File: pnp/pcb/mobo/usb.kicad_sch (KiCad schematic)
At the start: 5 parts, among them J9 USB_B, U8 SRV05-4

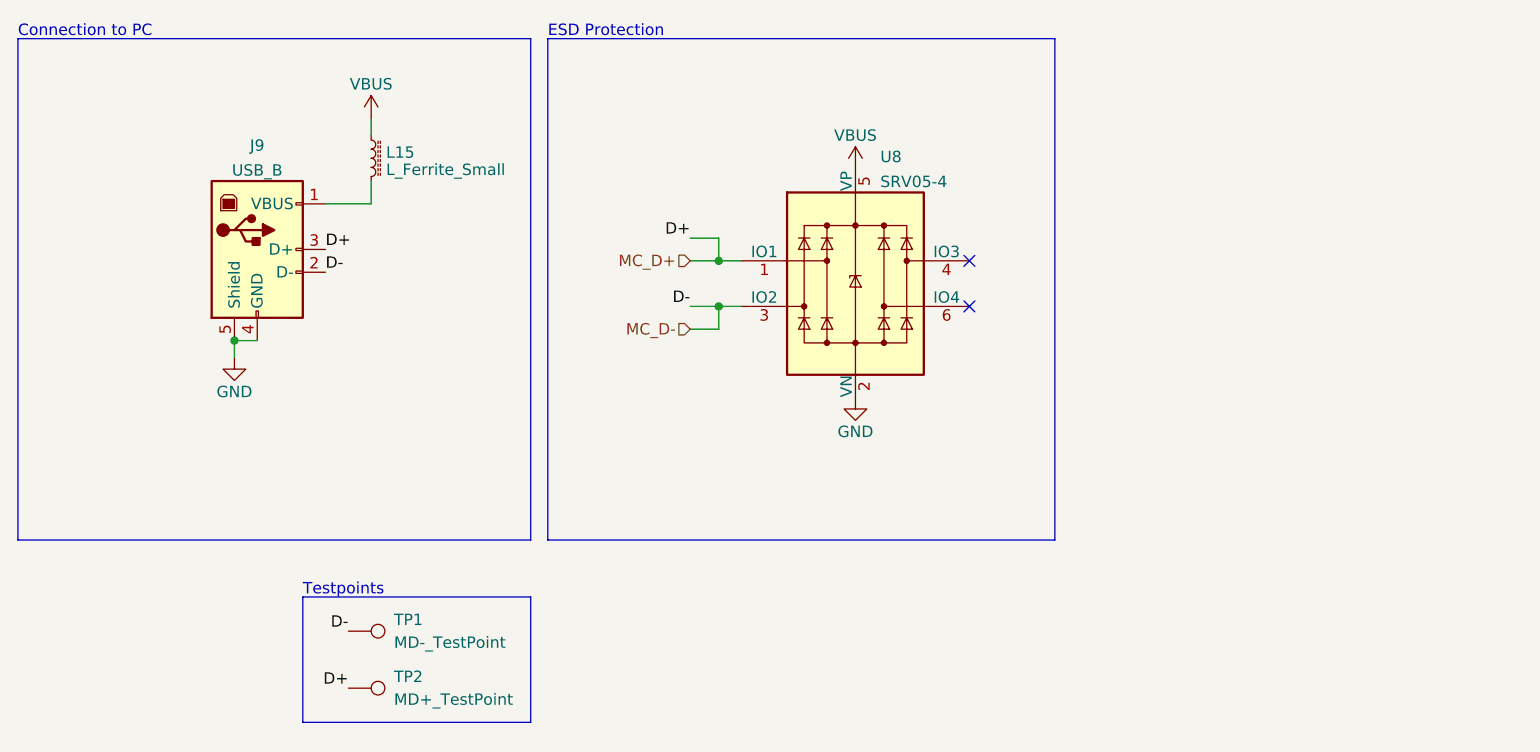
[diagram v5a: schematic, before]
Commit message: Replaced solder jumpers with 0ohm
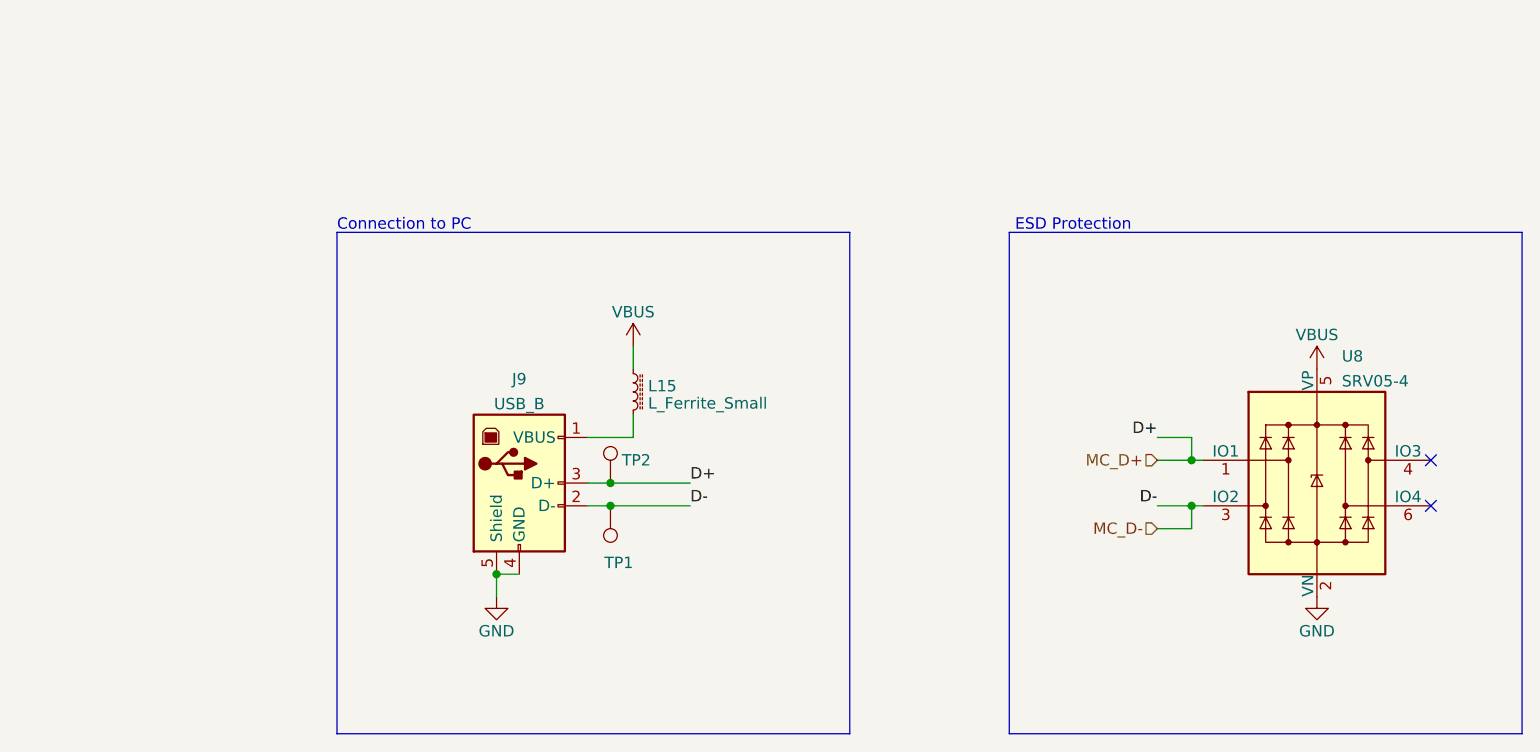
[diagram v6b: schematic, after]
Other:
- note removed: "Testpoints"
- moved on the sheet: J9, L15, TP1, TP2, U8

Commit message: Motor driver new Symbol and fix TVS placement
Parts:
- L15: footprint index:L_0805_2012Metric -> Inductor_SMD:L_0805_2012Metric
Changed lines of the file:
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@@
   (title_block
     (title "LumenPnP Motherboard")
-    (date "2022-03-29")
-    (rev "003")
+    (date "2023-07-30")
+    (rev "005")
     (company "Opulo")
+    (comment 1 "USB")
   )
   (junction (at 116.84 101.6) (diameter 0) (color 0 0 0 0)
@@
       (effects (font (size 1.27 1.27)) (justify left))
     )
-    (property "Footprint" "index:L_0805_2012Metric" (at 119.38 91.44 0)
-      (effects (font (size 1.27 1.27)) hide)
-    )
+    (property "Footprint" "Inductor_SMD:L_0805_2012Metric" (at 119.38 91.44 0)
+      (effects (font (size 1.27 1.27)) hide)
+    )

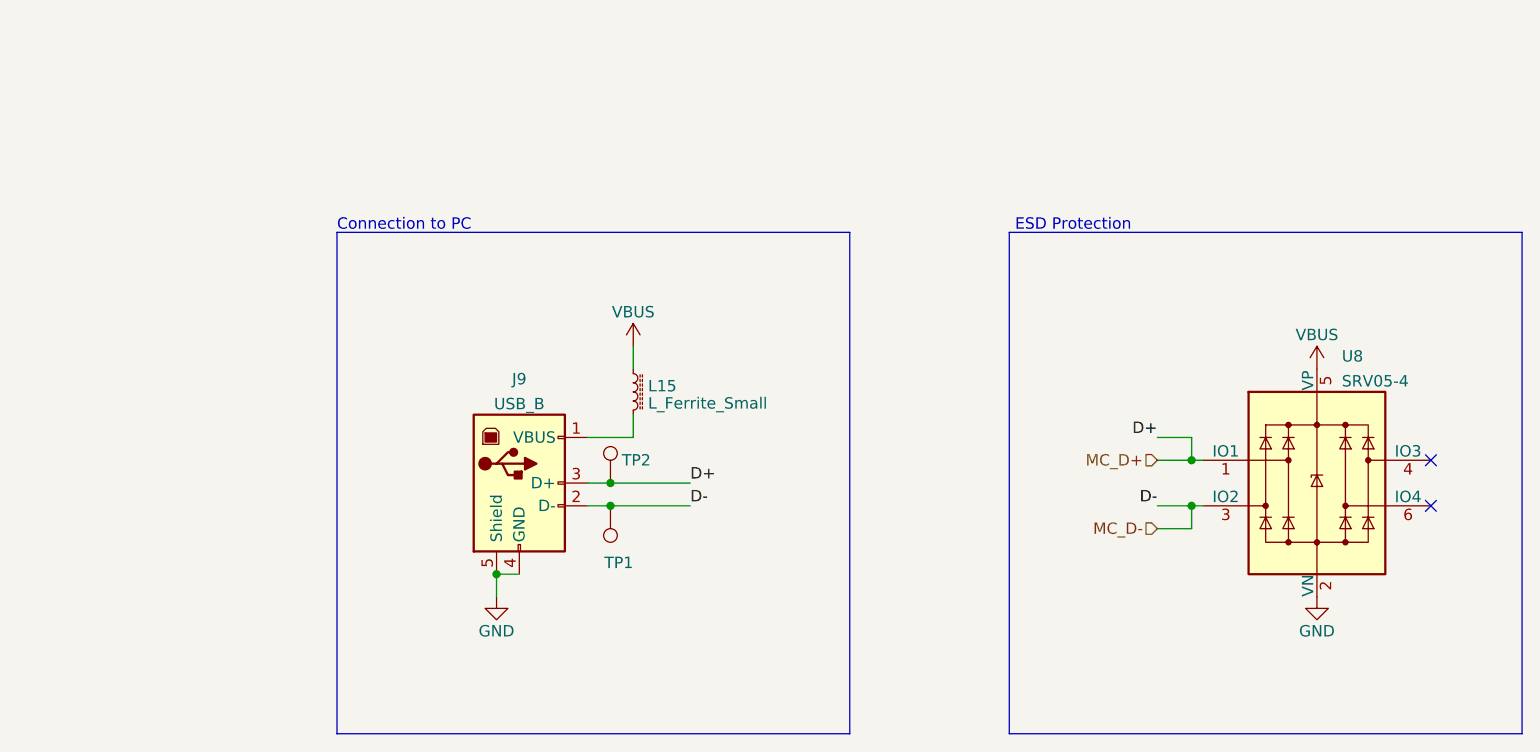
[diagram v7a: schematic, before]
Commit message: Add link to check symbol approval status
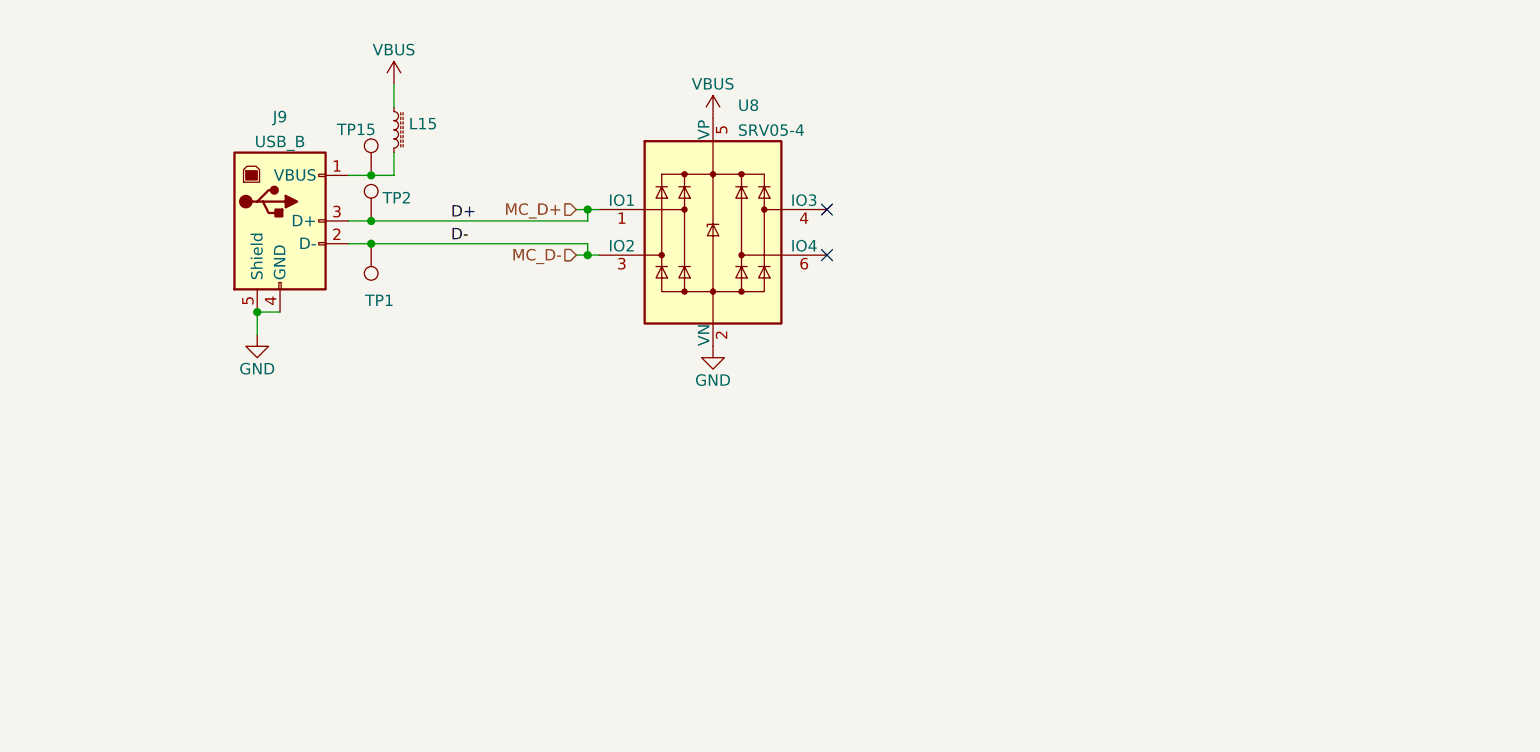
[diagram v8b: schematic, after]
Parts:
- added TP15: MD+_TestPoint, TestPoint:TestPoint_Pad_D2.0mm, symbol Connector:TestPoint
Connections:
- net at J9.1 (VBUS), L15.2: now also TP15.1
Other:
- note removed: "Connection to PC"
- note removed: "ESD Protection"
- moved on the sheet: J9, L15, TP1, TP2, U8
